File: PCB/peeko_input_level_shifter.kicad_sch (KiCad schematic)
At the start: 21 parts, among them J1 Conn_02x15_Odd_Even, J2 Conn_02x15_Odd_Even, U1 TXU0104, U2 TXU0104, U3 TXU0104, U4 TXU0104, U5 TXU0104, U6 TXU0104

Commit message: shrink level shifter
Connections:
- net +5V: now also JP1.1 (A); no longer JP1.2 (B)
- net VREF: now also JP1.2 (B); no longer JP1.1 (A)
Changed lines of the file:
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@@
 		(lib_id "000_LOCAL:Jumper_2_Bridged")
 		(at 215.9 82.55 0)
+		(mirror y)
 		(unit 1)
 		(exclude_from_sim yes)
@@
 		(on_board yes)
 		(dnp no)
-		(fields_autoplaced yes)
 		(property "Reference" "JP1"
 			(at 215.9 77.47 0)

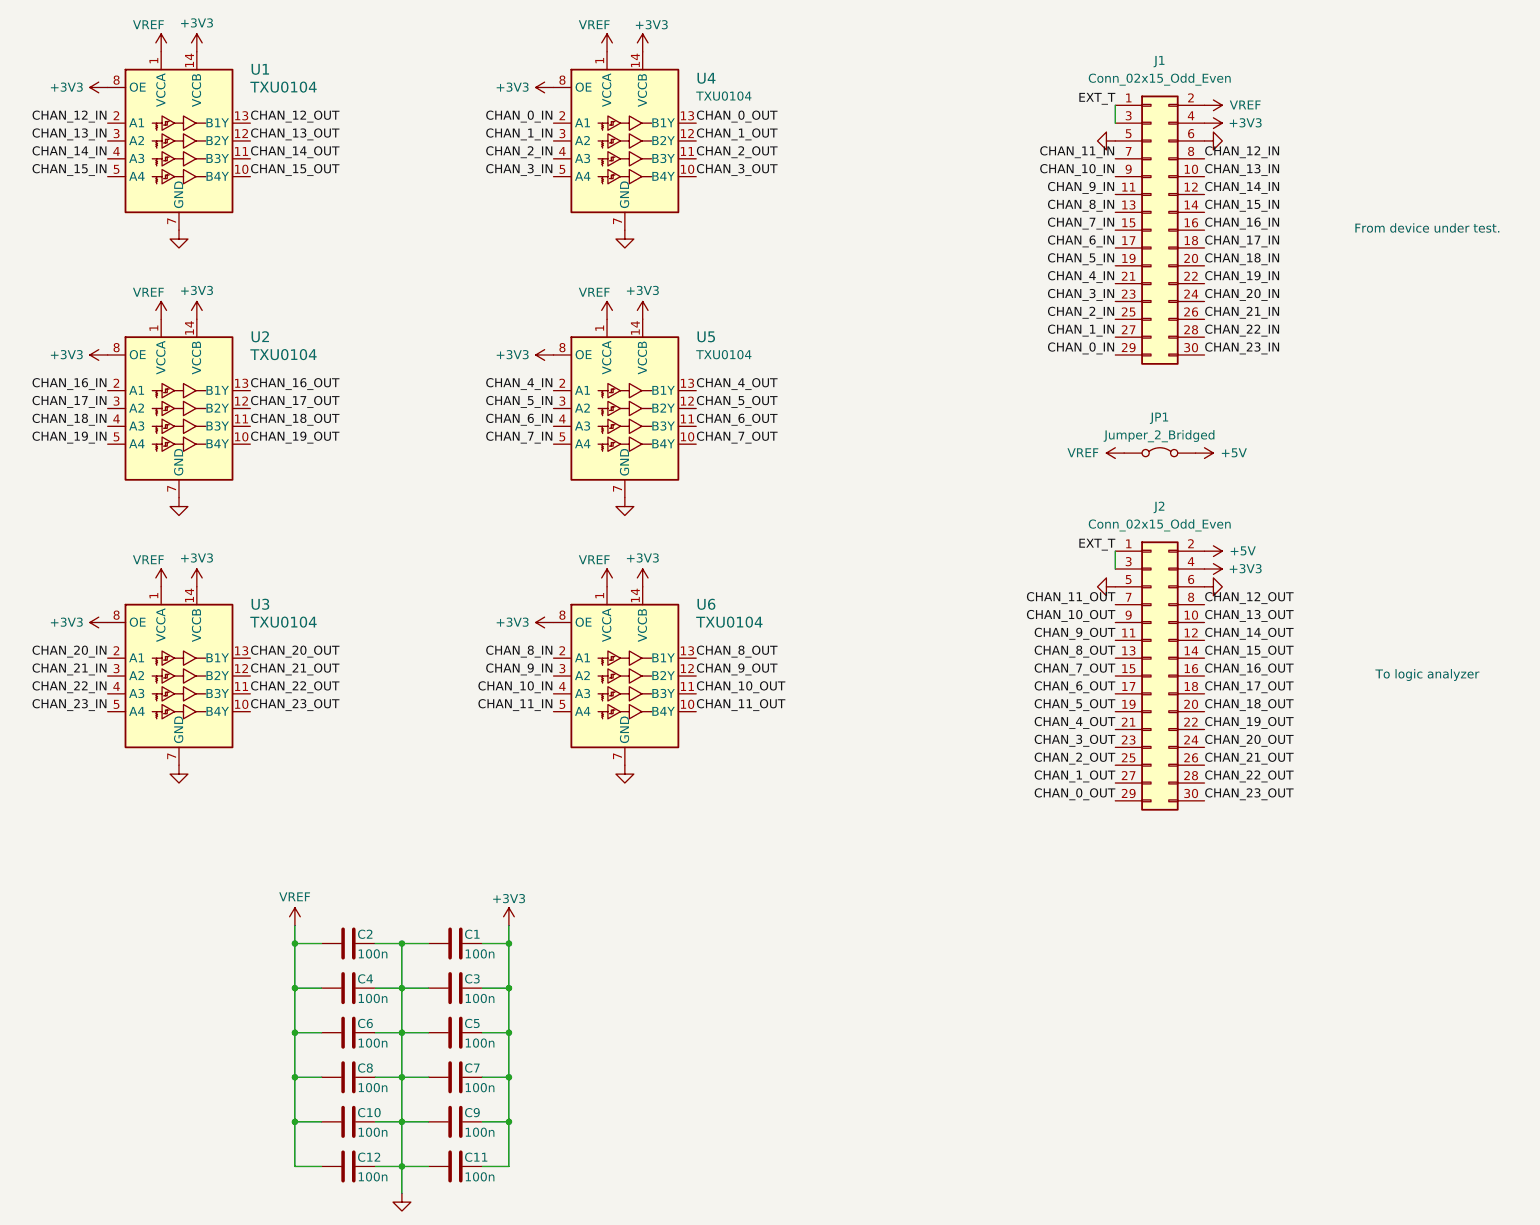
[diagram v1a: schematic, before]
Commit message: renumber level shifter
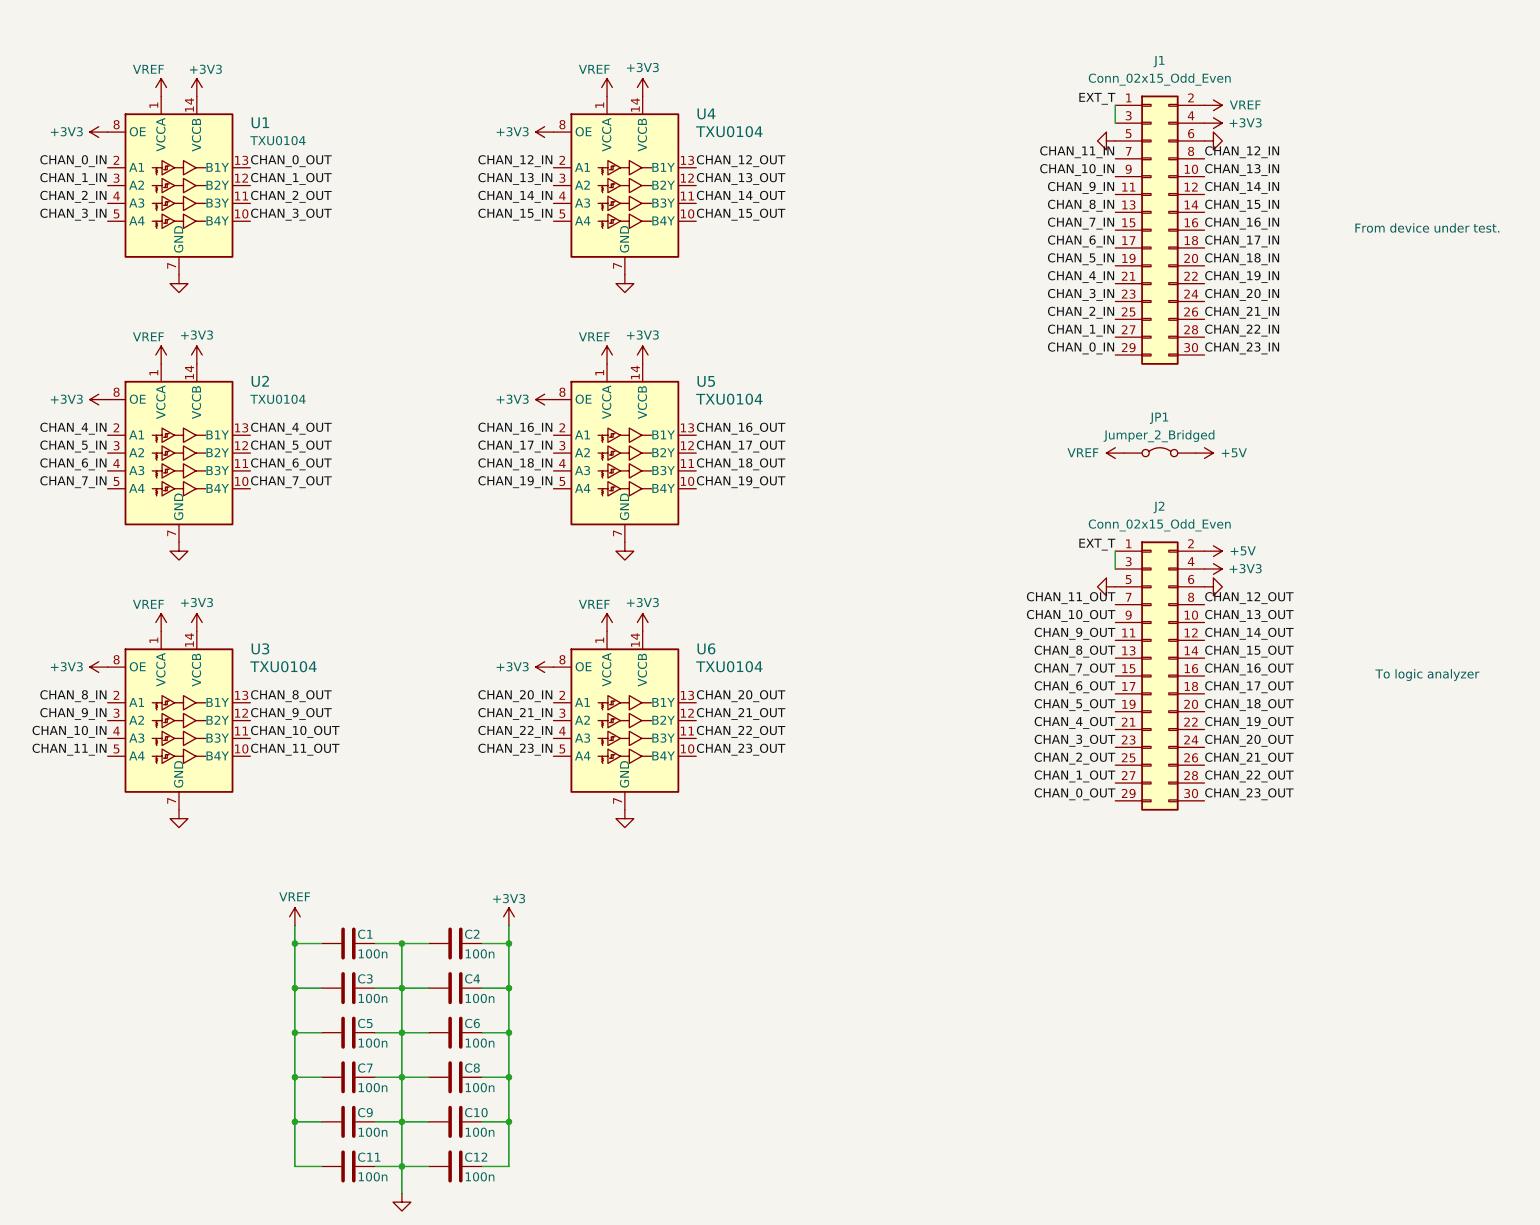
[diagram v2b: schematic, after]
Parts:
- renumbered U4 to U1, U5 to U2, U6 to U3, U1 to U4, U2 to U5, U3 to U6
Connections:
- net +3V3: now also C10.1, C12.1, C2.1, C4.1, C6.1, C8.1; no longer C1.1, C11.1, C3.1, C5.1, C7.1, C9.1
- net GND: now also C1.1, C10.2, C11.1, C12.2, C2.2, C3.1, C4.2, C5.1, C6.2, C7.1, C8.2, C9.1; no longer C1.2, C10.1, C11.2, C12.1, C2.1, C3.2, C4.1, C5.2, C6.1, C7.2, C8.1, C9.2
- net VREF: now also C1.2, C11.2, C3.2, C5.2, C7.2, C9.2; no longer C10.2, C12.2, C2.2, C4.2, C6.2, C8.2
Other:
- moved on the sheet: C1, C10, C11, C12, C2, C3, C4, C5, C6, C7, C8, C9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

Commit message: local tssop14 footprint, redo short side traces on peeko+ & level shifter
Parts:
- JP1: footprint 000_LOCAL:PinHeader_1x02_P2.54mm_Horizontal -> 000_LOCAL:PinHeader_1x02_P2.54mm_Horizontal jumper closed
- U1, U2, U3, U4, U5, U6: footprint Package_SO:TSSOP-14_4.4x5mm_P0.65mm -> 000_LOCAL:TSSOP-14_4.4x5mm_P0.65mm
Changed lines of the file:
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@@
 			)
 		)
-		(property "Footprint" "Package_SO:TSSOP-14_4.4x5mm_P0.65mm"
+		(property "Footprint" "000_LOCAL:TSSOP-14_4.4x5mm_P0.65mm"
 			(at 76.2 87.63 0)
 			(effects
@@
 			)
 		)
-		(property "Footprint" "Package_SO:TSSOP-14_4.4x5mm_P0.65mm"
+		(property "Footprint" "000_LOCAL:TSSOP-14_4.4x5mm_P0.65mm"
 			(at 76.2 49.53 0)
 			(effects
@@
 			)
 		)
-		(property "Footprint" "000_LOCAL:PinHeader_1x02_P2.54mm_Horizontal"
+		(property "Footprint" "000_LOCAL:PinHeader_1x02_P2.54mm_Horizontal jumper closed"
 			(at 215.9 82.55 0)
 			(effects
@@
 			)
 		)
-		(property "Footprint" "Package_SO:TSSOP-14_4.4x5mm_P0.65mm"
+		(property "Footprint" "000_LOCAL:TSSOP-14_4.4x5mm_P0.65mm"
 			(at 139.7 87.63 0)
 			(effects
@@
 			)
 		)
-		(property "Footprint" "Package_SO:TSSOP-14_4.4x5mm_P0.65mm"
+		(property "Footprint" "000_LOCAL:TSSOP-14_4.4x5mm_P0.65mm"
 			(at 139.7 49.53 0)
 			(effects
@@
 			)
 		)
-		(property "Footprint" "Package_SO:TSSOP-14_4.4x5mm_P0.65mm"
+		(property "Footprint" "000_LOCAL:TSSOP-14_4.4x5mm_P0.65mm"
 			(at 76.2 125.73 0)
 			(effects
@@
 			)
 		)
-		(property "Footprint" "Package_SO:TSSOP-14_4.4x5mm_P0.65mm"
+		(property "Footprint" "000_LOCAL:TSSOP-14_4.4x5mm_P0.65mm"
 			(at 139.7 125.73 0)
 			(effects
